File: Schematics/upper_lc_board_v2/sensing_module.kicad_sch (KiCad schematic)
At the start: 13 parts, among them J5 HALL-1, U7 ADC_ADS131M04IPWR

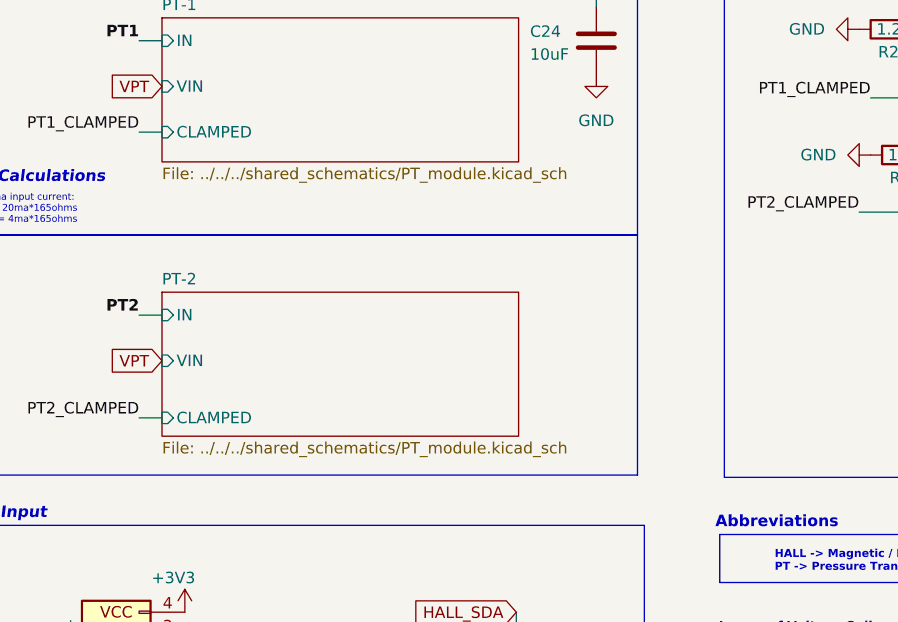
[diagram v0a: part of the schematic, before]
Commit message: layout updates after review, cleaned up schematic organization
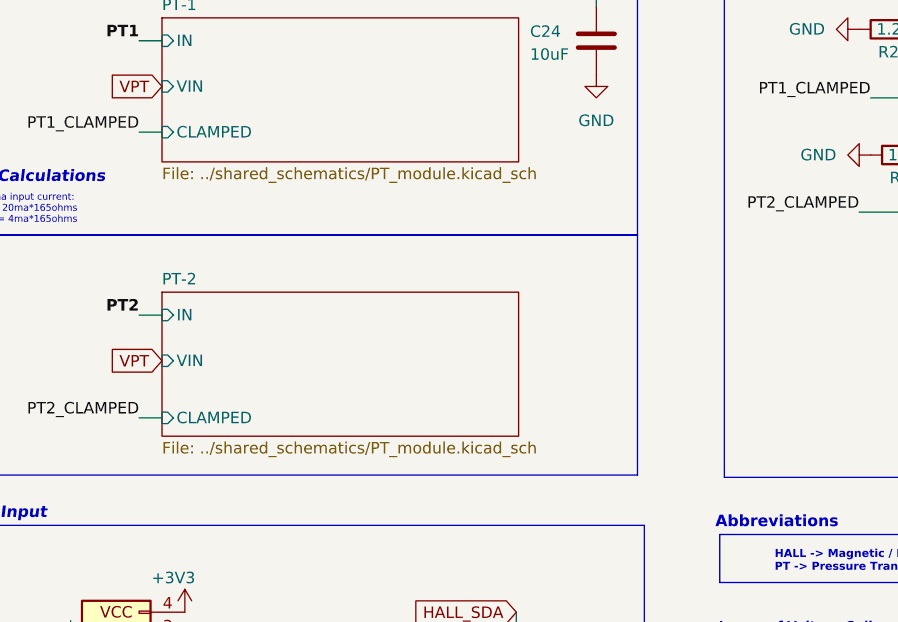
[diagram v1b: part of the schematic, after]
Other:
- sheet PT-1: file ../../../shared_schematics/PT_module.kicad_sch -> ../shared_schematics/PT_module.kicad_sch
- sheet PT-2: file ../../../shared_schematics/PT_module.kicad_sch -> ../shared_schematics/PT_module.kicad_sch
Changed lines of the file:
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@@
 		)
 		(instances
-			(project ""
+			(project "upper_lc_board_v2"
 				(path "/8de962ac-ee95-4233-a205-efbcd04063bc/32a8ecec-3c56-4fc7-b1a3-95683e41c1c6"
 					(reference "#PWR064")
@@
 			)
 		)
-		(property "Sheetfile" "../../../shared_schematics/PT_module.kicad_sch"
+		(property "Sheetfile" "../shared_schematics/PT_module.kicad_sch"
 			(at 76.2 71.1966 0)
 			(effects
@@
 			)
 		)
-		(property "Sheetfile" "../../../shared_schematics/PT_module.kicad_sch"
+		(property "Sheetfile" "../shared_schematics/PT_module.kicad_sch"
 			(at 76.2 101.6766 0)
 			(effects

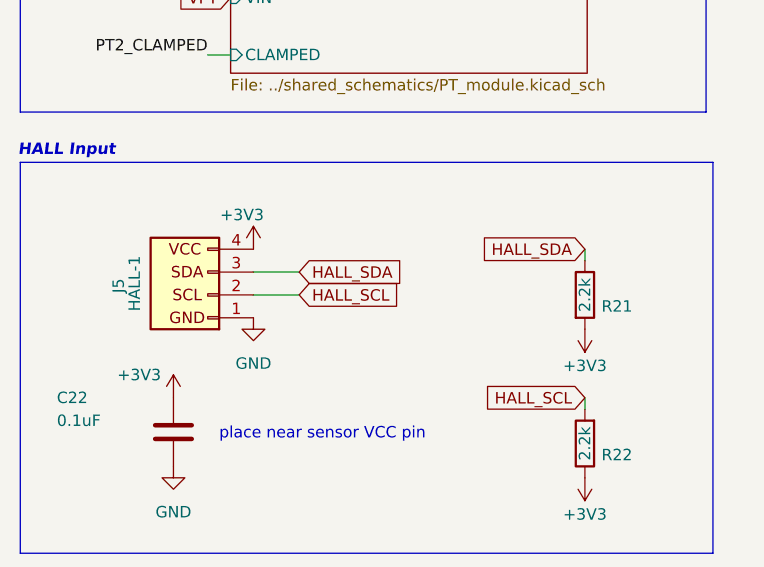
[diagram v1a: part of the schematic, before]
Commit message: swap I2C lines, add digi numbers to conns, fix diode issue
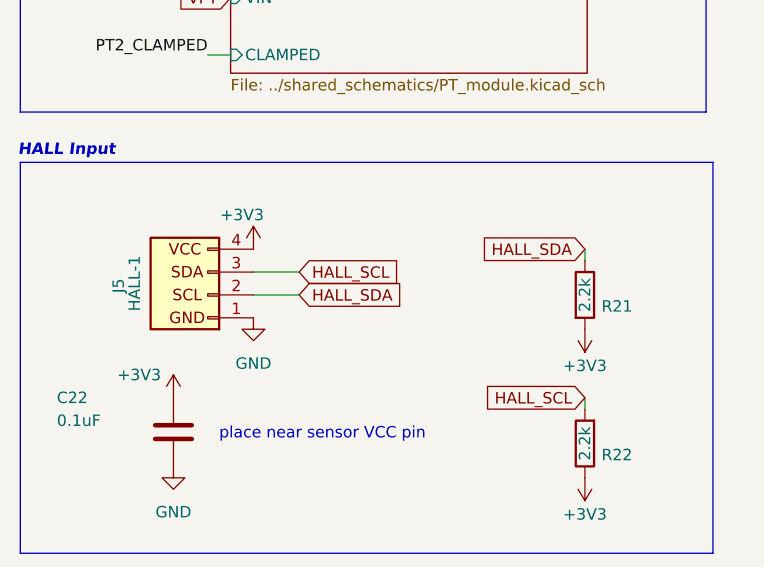
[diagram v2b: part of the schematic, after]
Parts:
- J5: Digikey 455-S04B-PASK-2-ND -> WM16895-ND
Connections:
- net HALL_SCL: now also J5.3 (Pin_3); no longer J5.2 (Pin_2)
- net HALL_SDA: now also J5.2 (Pin_2); no longer J5.3 (Pin_3)
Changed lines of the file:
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@@
-		)
-	)
-	(global_label "HALL_SDA"
-		(shape input)
-		(at 83.82 123.19 0)
-		(fields_autoplaced yes)
-		(effects
-			(font
-				(size 1.27 1.27)
-			)
-			(justify left)
-		)
-		(property "Intersheetrefs" "${INTERSHEET_REFS}"
-			(at 95.8162 123.19 0)
-			(effects
-				(font
-					(size 1.27 1.27)
-				)
-				(justify left)
-				(hide yes)
-			)
 		)
 	)
@@
 		)
 	)
-	(global_label "HALL_SCL"
+	(global_label "HALL_SDA"
 		(shape input)
 		(at 83.82 125.73 0)
@@
 		)
 		(property "Intersheetrefs" "${INTERSHEET_REFS}"
-			(at 95.7557 125.73 0)
+			(at 95.8162 125.73 0)
+			(effects
+				(font
+					(size 1.27 1.27)
+				)
+				(justify left)
+				(hide yes)
+			)
+		)
+	)
+	(global_label "HALL_SCL"
+		(shape input)
+		(at 83.82 123.19 0)
+		(fields_autoplaced yes)
+		(effects
+			(font
+				(size 1.27 1.27)
+			)
+			(justify left)
+		)
+		(property "Intersheetrefs" "${INTERSHEET_REFS}"
+			(at 95.7557 123.19 0)
 			(effects
 				(font
@@
 			)
 		)
-		(property "Digikey" "455-S04B-PASK-2-ND"
+		(property "Digikey" "WM16895-ND"
 			(at 73.66 125.73 90)
 			(effects

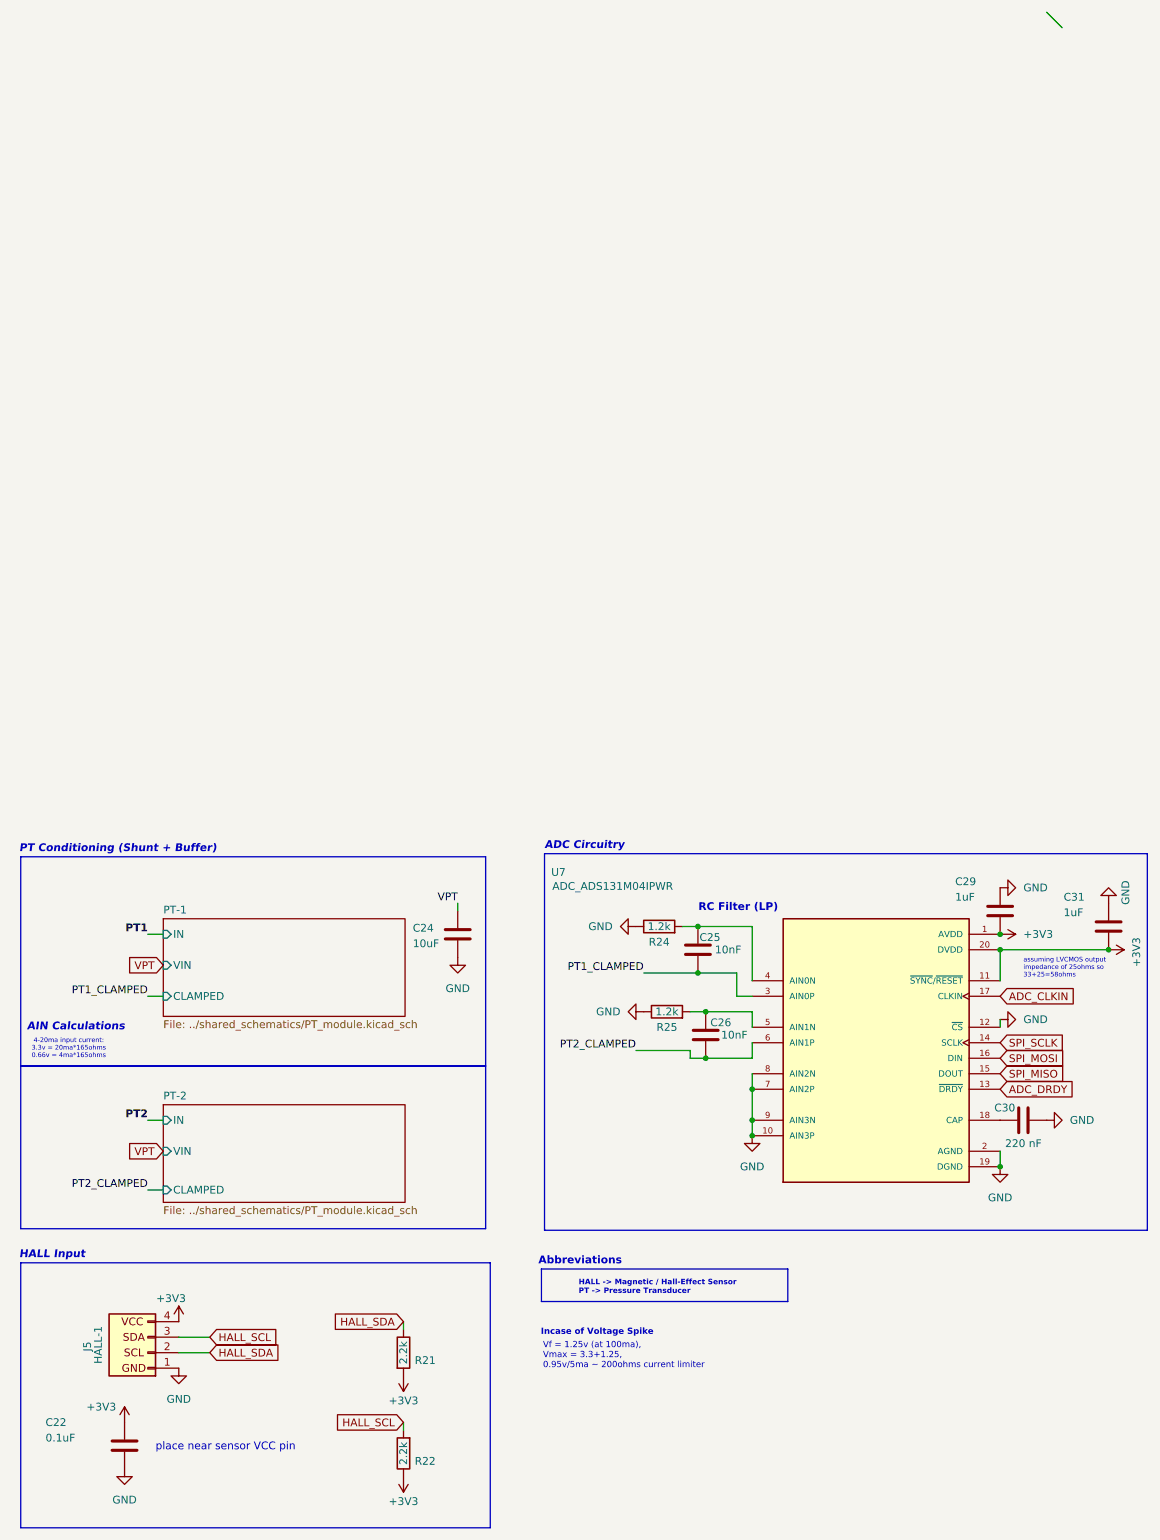
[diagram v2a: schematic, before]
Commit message: updated part numbers and fixed minor circuit issues
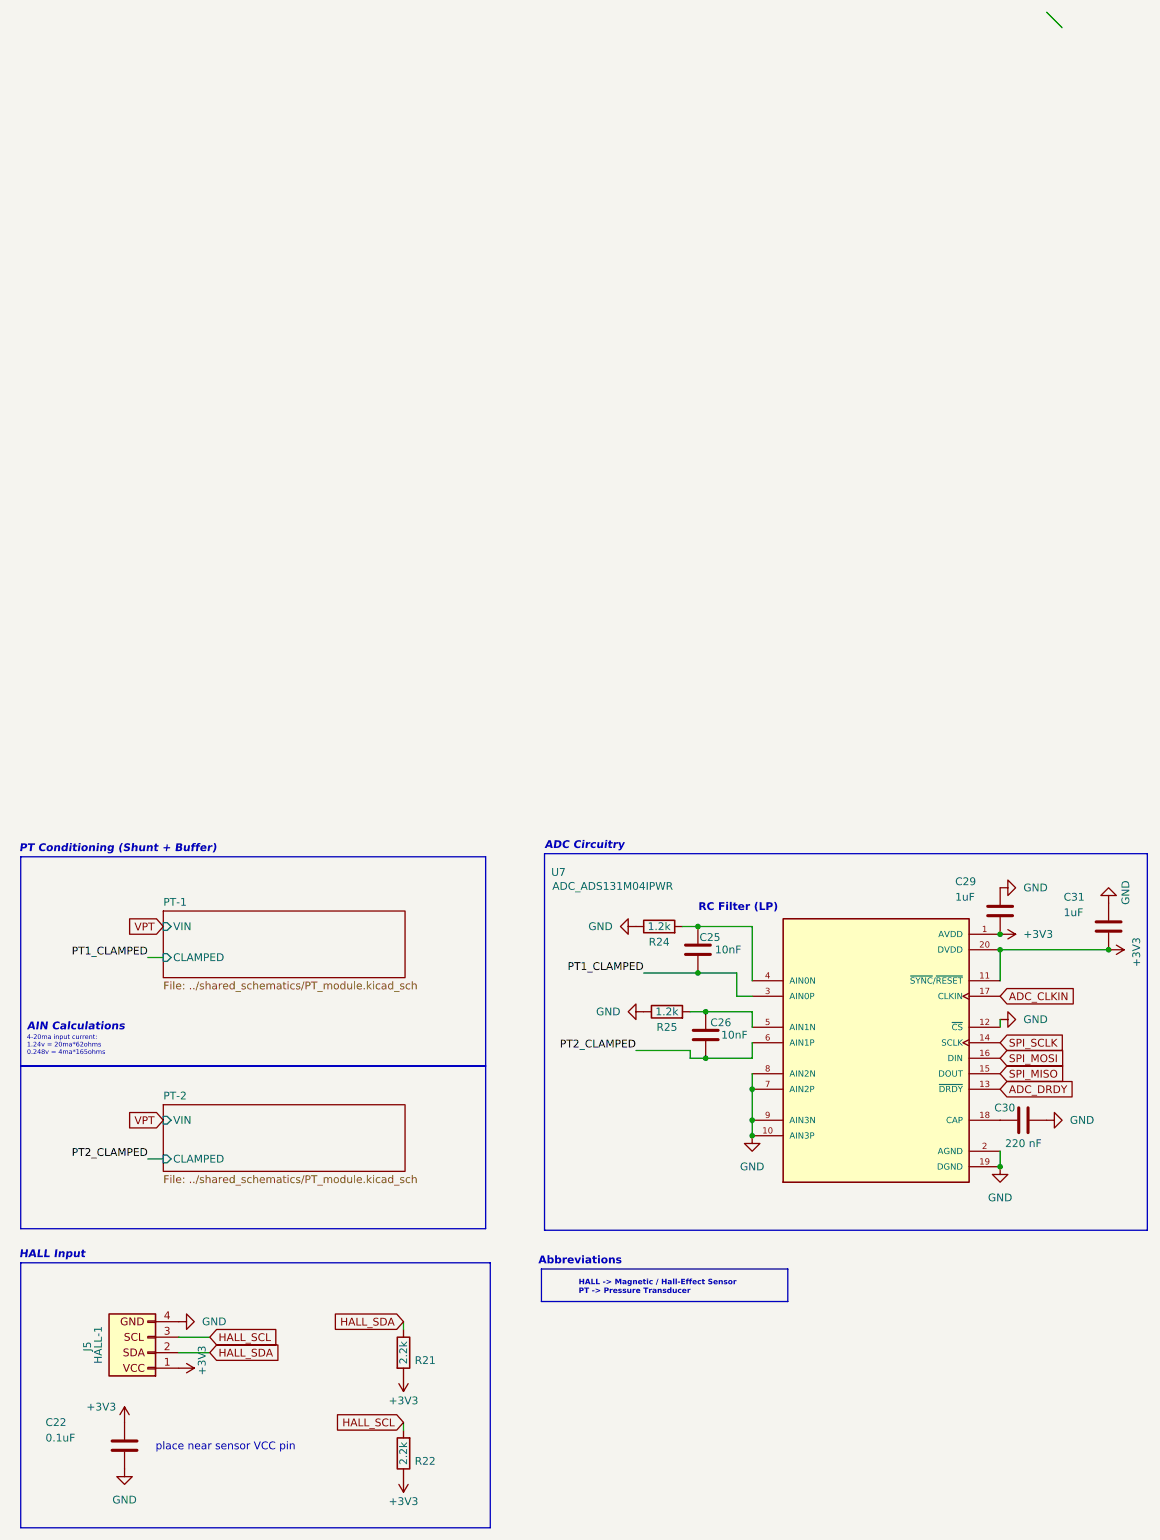
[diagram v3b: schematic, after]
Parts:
- removed C24: 10uF, Capacitor_SMD:C_1206_3216Metric, symbol Device:C
- C22: JLCPCB C49678 -> (none); LCSC (none) -> C49678
- C25, C26: LCSC C76599 -> C57112
- C29, C31: JLCPCB C15849 -> (none)
- C30: LCSC C5378 -> C21120
- U7: Price None -> (none); SnapEDA_Link https://www.snapeda.com/parts/ADS131M04IPWR/Texas+Instrumen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 -> (none)
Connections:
- net +3V3: now also J5.1 (Pin_1); no longer J5.4 (Pin_4)
- net GND: now also J5.4 (Pin_4); no longer J5.1 (Pin_1)
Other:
- sheet PT-1 ports: added none; removed IN
- sheet PT-2 ports: added none; removed IN
- note added: "4-20ma input current: 1.24v = 20ma*62ohms 0.248v = 4ma*165ohms"
- note removed: "4-20ma input current: 3.3v = 20ma*165ohms 0.66v = 4ma*165ohms"
- note removed: "Incase of Voltage Spike"
- note removed: "Vf = 1.25v (at 100ma), Vmax = 3.3+1.25, 0.95v/5ma ~ 200ohms current limiter"
- note removed: "assuming LVCMOS output impedance of 25ohms so 33+25=58ohms"
